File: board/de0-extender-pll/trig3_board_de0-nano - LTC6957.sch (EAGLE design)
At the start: 94 parts, among them IC1 FT230XQ, J12 4p-2.54, J13 BU-SMB-V, J17 2p-2.54, J23 2p-2.54, J24 2p-2.54, J32 2p-2.54, J34 2p-2.54, J38 2p-2.54, J42 2p-2.54, J43 2p-2.54, J7 4p-2.54, K15_P BU-SMB-V, K16N BU-SMB-V, P11 BU-SMB-V, P15 BU-SMB-V, P16_R15N BU-SMB-V, P9 BU-SMB-V, T13_B20N BU-SMB-V, U1 LTC6957IDD-2TRPBF

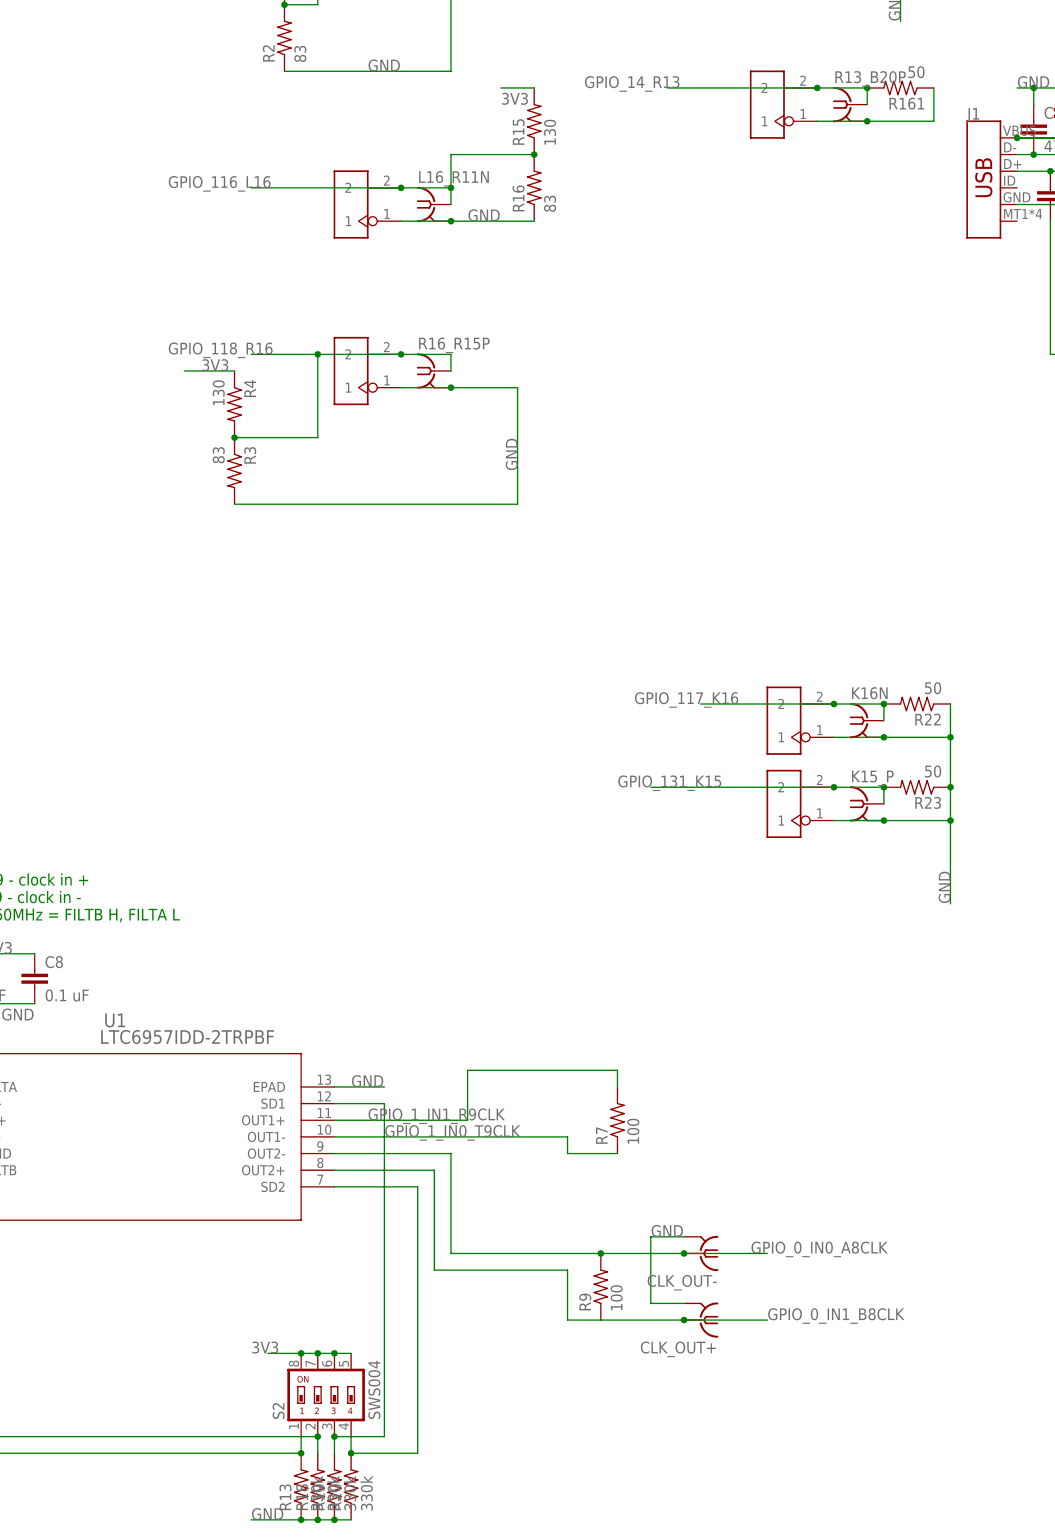
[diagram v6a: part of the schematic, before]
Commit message: fixed auto-router top layer nonsense
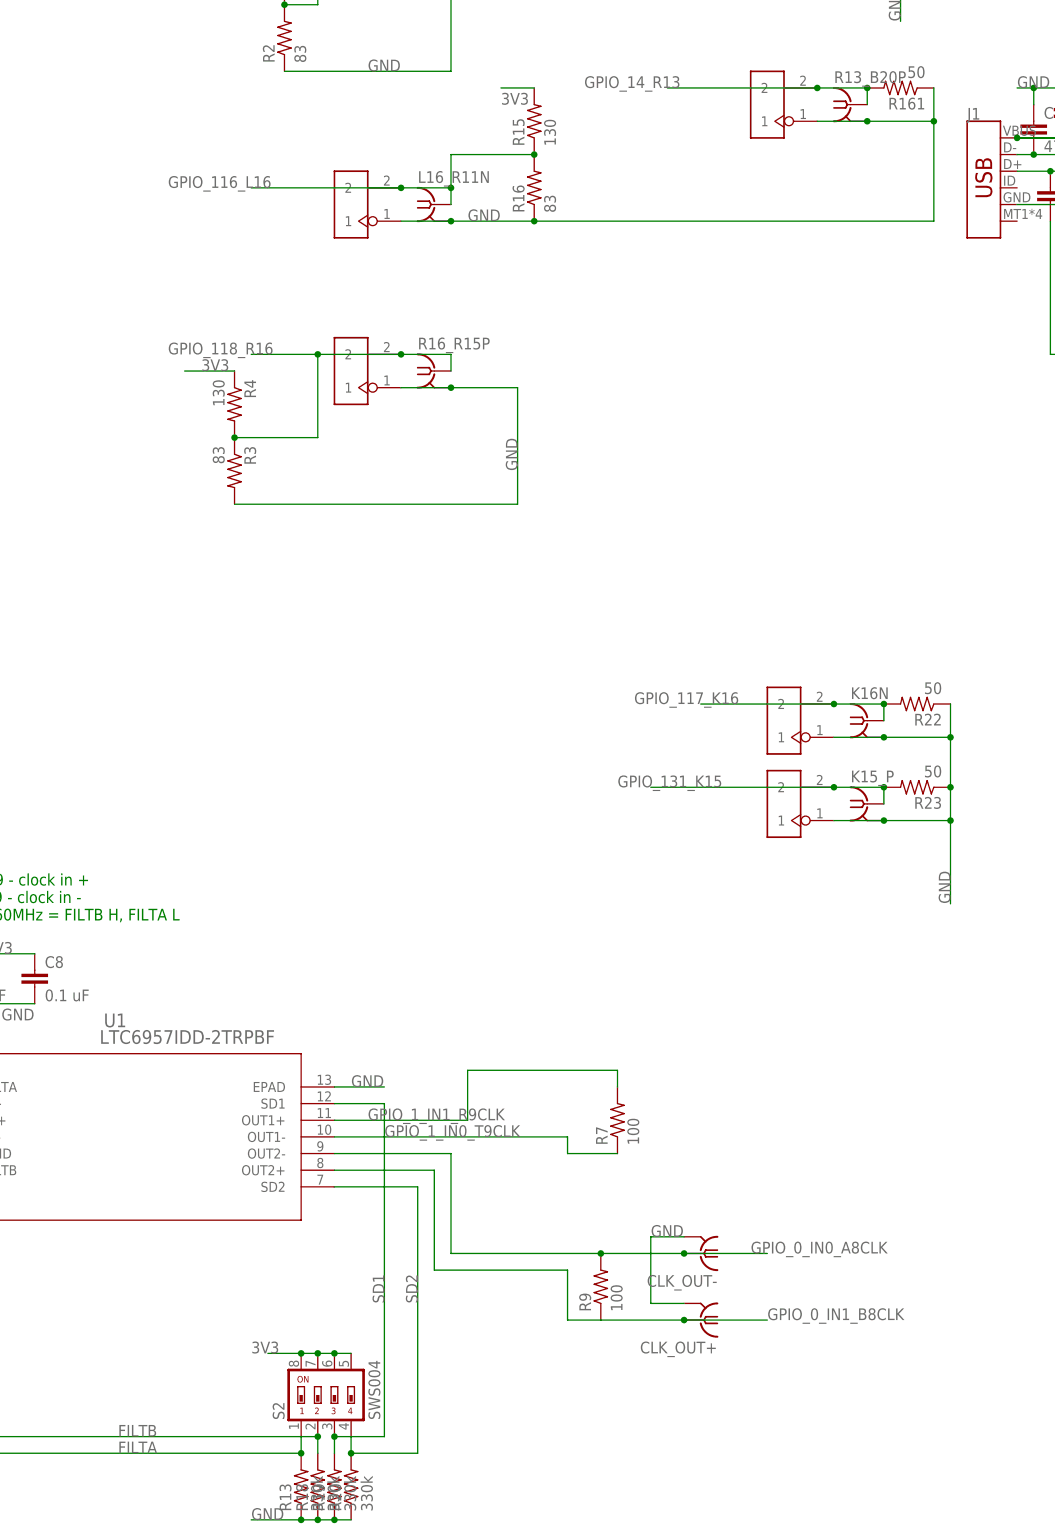
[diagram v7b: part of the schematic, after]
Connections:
- net N$15 renamed FILTA
- net N$16 renamed FILTB
- net N$17 renamed SD1
- net N$18 renamed SD2
- removed net N$1: J17.1, R13_B20P.2, R161.1
- net GND: now also J17.1, R13_B20P.2, R161.1
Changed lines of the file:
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@@
 <junction x="-63.5" y="165.1"/>
 <label x="-60.96" y="165.1" size="1.778" layer="95"/>
+<pinref part="R13_B20P" gate="G1" pin="2"/>
+<junction x="0" y="180.34"/>
+<pinref part="R161" gate="G$1" pin="1"/>
+<wire x1="10.16" y1="185.42" x2="10.16" y2="180.34" width="0.1524" layer="91"/>
+<wire x1="10.16" y1="180.34" x2="0" y2="180.34" width="0.1524" layer="91"/>
+<pinref part="J17" gate="G$1" pin="1"/>
+<wire x1="-7.62" y1="180.34" x2="0" y2="180.34" width="0.1524" layer="91"/>
+<wire x1="-50.8" y1="165.1" x2="10.16" y2="165.1" width="0.1524" layer="91"/>
+<wire x1="10.16" y1="165.1" x2="10.16" y2="180.34" width="0.1524" layer="91"/>
+<junction x="-50.8" y="165.1"/>
+<junction x="10.16" y="180.34"/>
 </segment>
 <segment>
@@
 </segment>
 </net>
-<net name="N$1" class="0">
-<segment>
-<pinref part="R13_B20P" gate="G1" pin="2"/>
-<junction x="0" y="180.34"/>
-<pinref part="R161" gate="G$1" pin="1"/>
-<wire x1="10.16" y1="185.42" x2="10.16" y2="180.34" width="0.1524" layer="91"/>
-<wire x1="10.16" y1="180.34" x2="0" y2="180.34" width="0.1524" layer="91"/>
-<pinref part="J17" gate="G$1" pin="1"/>
-<wire x1="-7.62" y1="180.34" x2="0" y2="180.34" width="0.1524" layer="91"/>
-</segment>
-</net>
 <net name="N$2" class="0">
 <segment>
@@
 </segment>
 </net>
-<net name="N$15" class="0">
+<net name="FILTA" class="0">
 <segment>
 <pinref part="S2" gate="G$1" pin="1"/>
@@
 <wire x1="-147.32" y1="-22.86" x2="-86.36" y2="-22.86" width="0.1524" layer="91"/>
 <junction x="-86.36" y="-22.86"/>
-</segment>
-</net>
-<net name="N$16" class="0">
+<label x="-114.3" y="-22.86" size="1.778" layer="95"/>
+</segment>
+</net>
+<net name="FILTB" class="0">
 <segment>
 <pinref part="R18" gate="G$1" pin="2"/>
@@
 <wire x1="-142.24" y1="-20.32" x2="-142.24" y2="20.32" width="0.1524" layer="91"/>
 <junction x="-83.82" y="-20.32"/>
-</segment>
-</net>
-<net name="N$17" class="0">
+<label x="-114.3" y="-20.32" size="1.778" layer="95"/>
+</segment>
+</net>
+<net name="SD1" class="0">
 <segment>
 <pinref part="R19" gate="G$1" pin="2"/>
@@
 <wire x1="-73.66" y1="-20.32" x2="-81.28" y2="-20.32" width="0.1524" layer="91"/>
 <junction x="-81.28" y="-20.32"/>
-</segment>
-</net>
-<net name="N$18" class="0">
+<label x="-73.66" y="0" size="1.778" layer="95" rot="R90"/>
+</segment>
+</net>
+<net name="SD2" class="0">
 <segment>
 <pinref part="R20" gate="G$1" pin="2"/>
@@
 <wire x1="-68.58" y1="-22.86" x2="-78.74" y2="-22.86" width="0.1524" layer="91"/>
 <junction x="-78.74" y="-22.86"/>
-</segment>
-</net>
+<label x="-68.58" y="0" size="1.778" layer="95" rot="R90"/>
+</segment>
+</net>

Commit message: removed wire stubs, tried to fix package rotation
rotated footprints in library but change did not propagate to pcb
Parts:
- C10, C12: LCSC_PART# (none) -> C1671
- C2, C4, C96: device SparkFun-Capacitors:CAP-0805 -> rcl:C-EUC0603; LCSC_PART# (none) -> C14663
- R1, R14, R15, R4: LCSC_PART# (none) -> C22796
- R10, R12: LCSC_PART# (none) -> C25190
- R11, R16, R2, R3: value 83 -> 82; LCSC_PART# (none) -> C23255
- R13, R18, R19, R20: LCSC_PART# (none) -> C23137
- R8: LCSC_PART# (none) -> C28636
- U1: LCSC_PART# (none) -> C689878
- VSLUE5, VSLUE7, VSLUE9: LCSC_PART# (none) -> C2869480
- renumbered K15_P to K15P, R13_B20P to R13P, T13_B20N to T13N
